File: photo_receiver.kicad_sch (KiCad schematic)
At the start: 9 parts

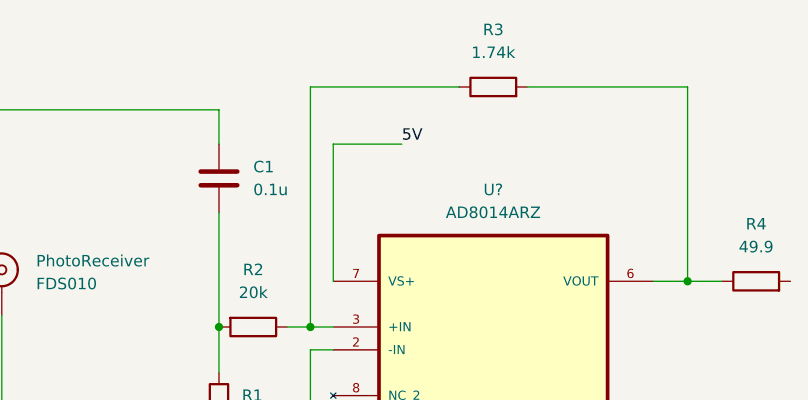
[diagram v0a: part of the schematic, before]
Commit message: Added power supply and standardised on pwer supply net names
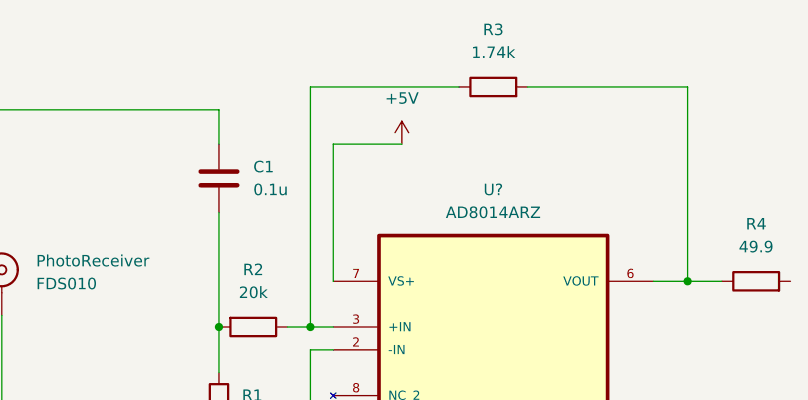
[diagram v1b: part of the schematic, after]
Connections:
- net 5V renamed +5V
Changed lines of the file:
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@@
     (stroke (width 0) (type default) (color 0 0 0 0))
-  )
-  (label "5V" (at 172.72 72.39 0)
-    (effects (font (size 1.27 1.27)) (justify left bottom))
   )
   (symbol (lib_id "local_library:AD8014ARZ") (at 182.88 95.25 0) (unit 1)
@@
     (pin "2")
   )
+  (symbol (lib_id "power:+5V") (at 172.72 72.39 0) (unit 1)
+    (in_bom yes) (on_board yes) (fields_autoplaced)
+    (property "Reference" "#PWR?" (id 0) (at 172.72 76.2 0)
+      (effects (font (size 1.27 1.27)) hide)
+    )
+    (property "Value" "+5V" (id 1) (at 172.72 67.31 0))
+    (property "Footprint" "" (id 2) (at 172.72 72.39 0)
+      (effects (font (size 1.27 1.27)) hide)
+    )
+    (property "Datasheet" "" (id 3) (at 172.72 72.39 0)
+      (effects (font (size 1.27 1.27)) hide)
+    )
+    (pin "1")
+  )
 )

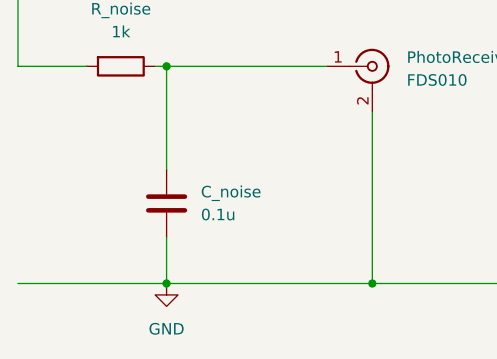
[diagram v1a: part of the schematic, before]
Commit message: improve labels on comparator
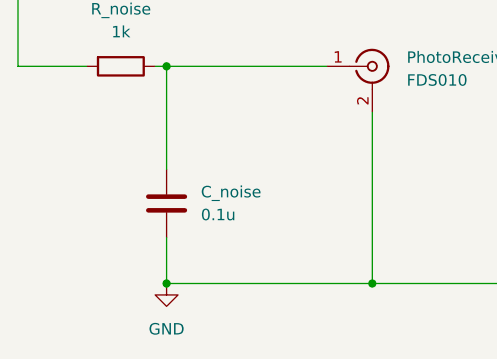
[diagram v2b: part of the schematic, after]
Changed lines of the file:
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@@
   (junction (at 105.41 86.36) (diameter 0) (color 0 0 0 0)
-  )
-  (wire (pts (xy 88.9 110.49) (xy 105.41 110.49))
-    (stroke (width 0) (type default) (color 0 0 0 0))
   )
   (wire (pts (xy 165.1 95.25) (xy 162.56 95.25))

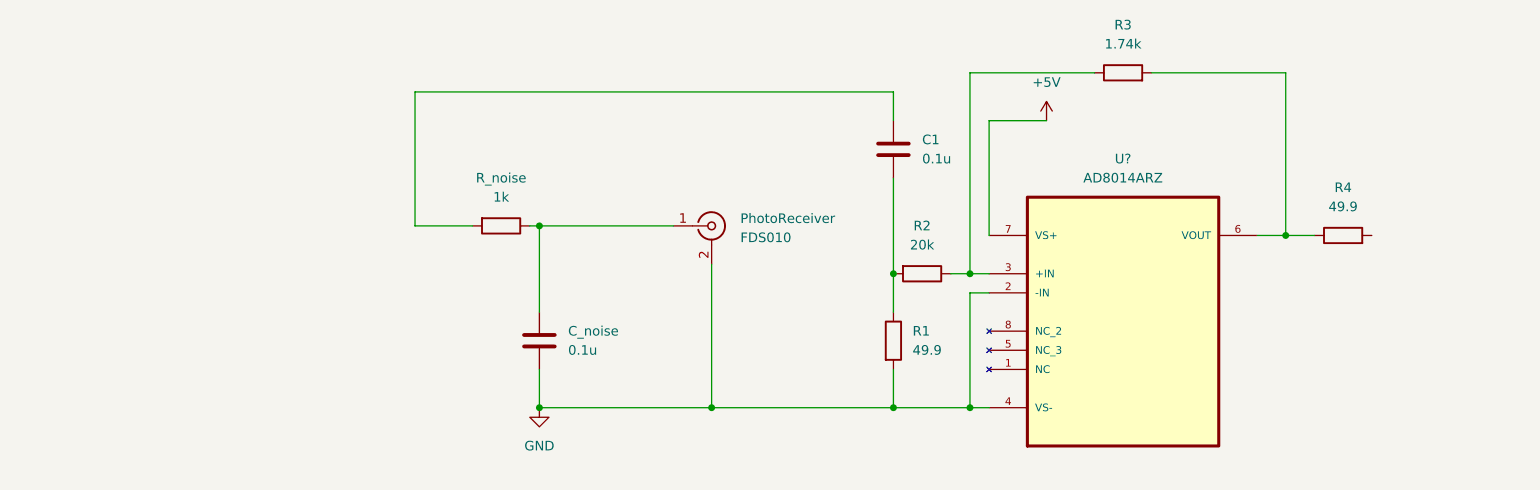
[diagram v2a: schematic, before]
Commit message: add component numbers to schematic
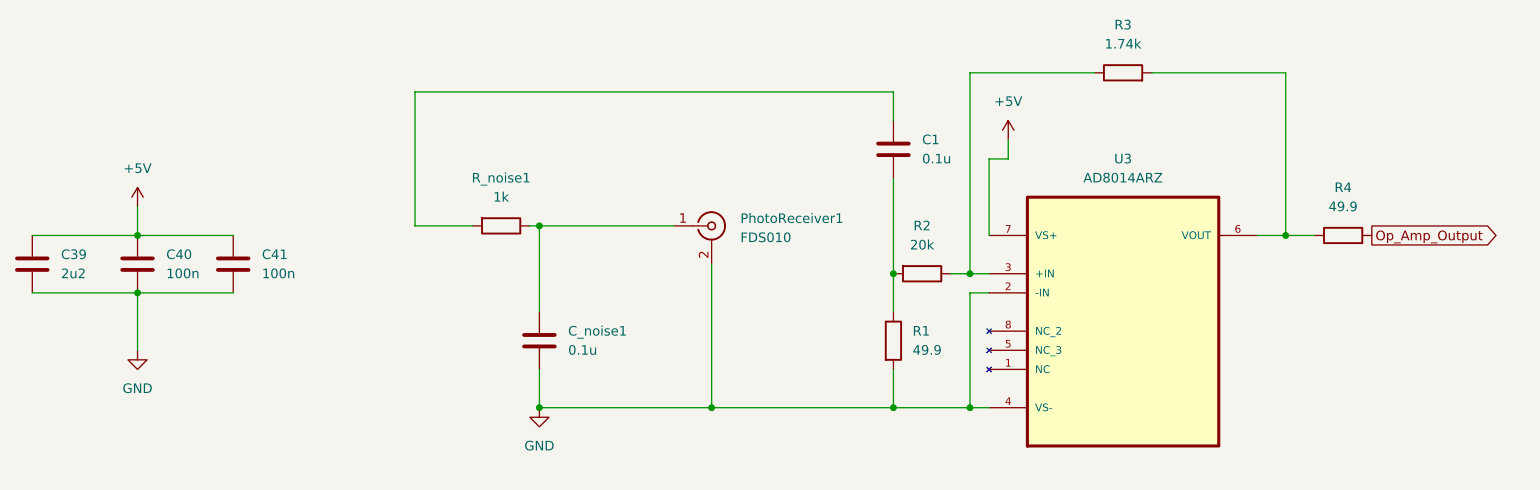
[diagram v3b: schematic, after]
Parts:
- added C39: 2u2, symbol Device:C
- added C40, C41: 100n, symbol Device:C
- gave numbers to parts that had none: 1
- renumbered C_noise to C_noise1, PhotoReceiver to PhotoReceiver1, R_noise to R_noise1
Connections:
- net +5V: now also C39.1, C40.1, C41.1
- net GND: now also C39.2, C40.2, C41.2
- net Op_Amp_Output: now reaches R4.2
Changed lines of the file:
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@@
 (kicad_sch (version 20211123) (generator eeschema)
   (paper "A4")
+  (junction (at 52.07 87.63) (diameter 0) (color 0 0 0 0)
+  )
   (junction (at 105.41 110.49) (diameter 0) (color 0 0 0 0)
   )
   (junction (at 162.56 110.49) (diameter 0) (color 0 0 0 0)
   )
+  (junction (at 52.07 95.25) (diameter 0) (color 0 0 0 0)
+  )
   (junction (at 152.4 110.49) (diameter 0) (color 0 0 0 0)
   )
@@
     (stroke (width 0) (type default) (color 0 0 0 0))
   )
+  (wire (pts (xy 167.64 77.47) (xy 165.1 77.47))
+    (stroke (width 0) (type default) (color 0 0 0 0))
+  )
   (wire (pts (xy 105.41 110.49) (xy 128.27 110.49))
     (stroke (width 0) (type default) (color 0 0 0 0))
@@
     (stroke (width 0) (type default) (color 0 0 0 0))
   )
+  (wire (pts (xy 52.07 83.82) (xy 52.07 87.63))
+    (stroke (width 0) (type default) (color 0 0 0 0))
+  )
   (wire (pts (xy 152.4 68.58) (xy 88.9 68.58))
     (stroke (width 0) (type default) (color 0 0 0 0))
   )
-  (wire (pts (xy 165.1 87.63) (xy 165.1 72.39))
-    (stroke (width 0) (type default) (color 0 0 0 0))
-  )
   (wire (pts (xy 105.41 86.36) (xy 123.19 86.36))
     (stroke (width 0) (type default) (color 0 0 0 0))
@@
     (stroke (width 0) (type default) (color 0 0 0 0))
   )
-  (wire (pts (xy 165.1 72.39) (xy 172.72 72.39))
+  (wire (pts (xy 167.64 74.93) (xy 167.64 77.47))
+    (stroke (width 0) (type default) (color 0 0 0 0))
+  )
+  (wire (pts (xy 52.07 87.63) (xy 64.77 87.63))
     (stroke (width 0) (type default) (color 0 0 0 0))
   )
@@
     (stroke (width 0) (type default) (color 0 0 0 0))
   )
+  (wire (pts (xy 38.1 87.63) (xy 52.07 87.63))
+    (stroke (width 0) (type default) (color 0 0 0 0))
+  )
   (wire (pts (xy 162.56 92.71) (xy 165.1 92.71))
     (stroke (width 0) (type default) (color 0 0 0 0))
@@
     (stroke (width 0) (type default) (color 0 0 0 0))
   )
+  (wire (pts (xy 52.07 95.25) (xy 52.07 102.87))
+    (stroke (width 0) (type default) (color 0 0 0 0))
+  )
   (wire (pts (xy 162.56 66.04) (xy 179.07 66.04))
     (stroke (width 0) (type default) (color 0 0 0 0))
@@
     (stroke (width 0) (type default) (color 0 0 0 0))
   )
+  (wire (pts (xy 38.1 95.25) (xy 52.07 95.25))
+    (stroke (width 0) (type default) (color 0 0 0 0))
+  )
   (wire (pts (xy 204.47 66.04) (xy 204.47 87.63))
     (stroke (width 0) (type default) (color 0 0 0 0))
   )
+  (wire (pts (xy 52.07 95.25) (xy 64.77 95.25))
+    (stroke (width 0) (type default) (color 0 0 0 0))
+  )
+  (wire (pts (xy 165.1 77.47) (xy 165.1 87.63))
+    (stroke (width 0) (type default) (color 0 0 0 0))
+  )
   (wire (pts (xy 128.27 110.49) (xy 152.4 110.49))
     (stroke (width 0) (type default) (color 0 0 0 0))
   )
+  (global_label "Op_Amp_Output" (shape output) (at 215.9 87.63 0) (fields_autoplaced)
+    (effects (font (size 1.27 1.27)) (justify left))
+    (property "Intersheet References" "${INTERSHEET_REFS}" (id 0) (at 232.8879 87.5506 0)
+      (effects (font (size 1.27 1.27)) (justify left) hide)
+    )
+  )
   (symbol (lib_id "local_library:AD8014ARZ") (at 182.88 95.25 0) (unit 1)
     (in_bom yes) (on_board yes) (fields_autoplaced)
-    (property "Reference" "U?" (id 0) (at 182.88 77.47 0))
+    (property "Reference" "U3" (id 0) (at 182.88 77.47 0))
     (property "Value" "AD8014ARZ" (id 1) (at 182.88 80.01 0))
     (property "Footprint" "SOIC127P600X175-8N" (id 2) (at 182.88 85.09 0)
@@
   (symbol (lib_id "power:GND") (at 105.41 110.49 0) (unit 1)
     (in_bom yes) (on_board yes) (fields_autoplaced)
-    (property "Reference" "#PWR?" (id 0) (at 105.41 116.84 0)
+    (property "Reference" "#PWR038" (id 0) (at 105.41 116.84 0)
       (effects (font (size 1.27 1.27)) hide)
     )
@@
     )
     (property "Datasheet" "~" (id 3) (at 152.4 76.2 0)
+      (effects (font (size 1.27 1.27)) hide)
+    )
+    (pin "1")
+    (pin "2")
+  )
+  (symbol (lib_id "Device:C") (at 64.77 91.44 0) (unit 1)
+    (in_bom yes) (on_board yes) (fields_autoplaced)
+    (property "Reference" "C41" (id 0) (at 68.58 90.1699 0)
+      (effects (font (size 1.27 1.27)) (justify left))
+    )
+    (property "Value" "100n" (id 1) (at 68.58 92.7099 0)
+      (effects (font (size 1.27 1.27)) (justify left))
+    )
+    (property "Footprint" "" (id 2) (at 65.7352 95.25 0)
+      (effects (font (size 1.27 1.27)) hide)
+    )
+    (property "Datasheet" "~" (id 3) (at 64.77 91.44 0)
       (effects (font (size 1.27 1.27)) hide)
     )
@@
   (symbol (lib_id "Connector:Conn_Coaxial") (at 128.27 86.36 0) (unit 1)
     (in_bom yes) (on_board yes) (fields_autoplaced)
-    (property "Reference" "PhotoReceiver" (id 0) (at 132.08 85.3831 0)
+    (property "Reference" "PhotoReceiver1" (id 0) (at 132.08 85.3831 0)
       (effects (font (size 1.27 1.27)) (justify left))
     )
@@
   (symbol (lib_id "Device:C") (at 105.41 101.6 0) (unit 1)
     (in_bom yes) (on_board yes) (fields_autoplaced)
-    (property "Reference" "C_noise" (id 0) (at 109.22 100.3299 0)
+    (property "Reference" "C_noise1" (id 0) (at 109.22 100.3299 0)
       (effects (font (size 1.27 1.27)) (justify left))
     )
@@
   (symbol (lib_id "Device:R") (at 100.33 86.36 270) (unit 1)
     (in_bom yes) (on_board yes) (fields_autoplaced)
-    (property "Reference" "R_noise" (id 0) (at 100.33 80.01 90))
+    (property "Reference" "R_noise1" (id 0) (at 100.33 80.01 90))
     (property "Value" "1k" (id 1) (at 100.33 82.55 90))
     (property "Footprint" "" (id 2) (at 100.33 84.582 90)
@@
     (pin "2")
   )
-  (symbol (lib_id "power:+5V") (at 172.72 72.39 0) (unit 1)
-    (in_bom yes) (on_board yes) (fields_autoplaced)
-    (property "Reference" "#PWR?" (id 0) (at 172.72 76.2 0)
-      (effects (font (size 1.27 1.27)) hide)
-    )
-    (property "Value" "+5V" (id 1) (at 172.72 67.31 0))
-    (property "Footprint" "" (id 2) (at 172.72 72.39 0)
-      (effects (font (size 1.27 1.27)) hide)
-    )
-    (property "Datasheet" "" (id 3) (at 172.72 72.39 0)
-      (effects (font (size 1.27 1.27)) hide)
-    )
+  (symbol (lib_id "Device:C") (at 52.07 91.44 0) (unit 1)
+    (in_bom yes) (on_board yes) (fields_autoplaced)
+    (property "Reference" "C40" (id 0) (at 55.88 90.1699 0)
+      (effects (font (size 1.27 1.27)) (justify left))
+    )
+    (property "Value" "100n" (id 1) (at 55.88 92.7099 0)
+      (effects (font (size 1.27 1.27)) (justify left))
+    )
+    (property "Footprint" "" (id 2) (at 53.0352 95.25 0)
+      (effects (font (size 1.27 1.27)) hide)
+    )
+    (property "Datasheet" "~" (id 3) (at 52.07 91.44 0)
+      (effects (font (size 1.27 1.27)) hide)
+    )
+    (pin "1")
+    (pin "2")
+  )
+  (symbol (lib_id "power:+5V") (at 52.07 83.82 0) (unit 1)
+    (in_bom yes) (on_board yes) (fields_autoplaced)
+    (property "Reference" "#PWR052" (id 0) (at 52.07 87.63 0)
+      (effects (font (size 1.27 1.27)) hide)
+    )
+    (property "Value" "+5V" (id 1) (at 52.07 78.74 0))
+    (property "Footprint" "" (id 2) (at 52.07 83.82 0)
+      (effects (font (size 1.27 1.27)) hide)
+    )
+    (property "Datasheet" "" (id 3) (at 52.07 83.82 0)
+      (effects (font (size 1.27 1.27)) hide)
+    )
+    (pin "1")
+  )
+  (symbol (lib_id "power:GND") (at 52.07 102.87 0) (unit 1)
+    (in_bom yes) (on_board yes) (fields_autoplaced)
+    (property "Reference" "#PWR053" (id 0) (at 52.07 109.22 0)
+      (effects (font (size 1.27 1.27)) hide)
+    )
+    (property "Value" "GND" (id 1) (at 52.07 107.95 0))
+    (property "Footprint" "" (id 2) (at 52.07 102.87 0)
+      (effects (font (size 1.27 1.27)) hide)
+    )
+    (property "Datasheet" "" (id 3) (at 52.07 102.87 0)
+      (effects (font (size 1.27 1.27)) hide)
+    )
+    (pin "1")
+  )
+  (symbol (lib_id "Device:C") (at 38.1 91.44 0) (unit 1)
+    (in_bom yes) (on_board yes) (fields_autoplaced)
+    (property "Reference" "C39" (id 0) (at 41.91 90.1699 0)
+      (effects (font (size 1.27 1.27)) (justify left))
+    )
+    (property "Value" "2u2" (id 1) (at 41.91 92.7099 0)
+      (effects (font (size 1.27 1.27)) (justify left))
+    )
+    (property "Footprint" "" (id 2) (at 39.0652 95.25 0)
+      (effects (font (size 1.27 1.27)) hide)
+    )
+    (property "Datasheet" "~" (id 3) (at 38.1 91.44 0)
+      (effects (font (size 1.27 1.27)) hide)
+    )
+    (pin "1")
+    (pin "2")
+  )
+  (symbol (lib_id "power:+5V") (at 167.64 74.93 0) (unit 1)
+    (in_bom yes) (on_board yes) (fields_autoplaced)
+    (property "Reference" "#PWR039" (id 0) (at 167.64 78.74 0)
+      (effects (font (size 1.27 1.27)) hide)
+    )
+    (property "Value" "+5V" (id 1) (at 167.64 69.85 0))
+    (property "Footprint" "" (id 2) (at 167.64 74.93 0)
+      (effects (font (size 1.27 1.27)) hide)
+    )
+    (property "Datasheet" "" (id 3) (at 167.64 74.93 0)
+      (effects (font (size 1.27 1.27)) hide)
+    )

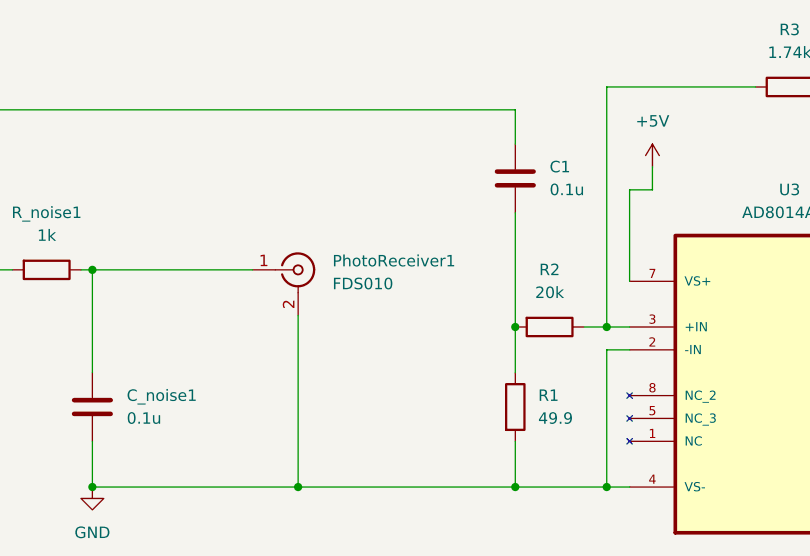
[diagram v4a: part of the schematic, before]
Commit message: Add footprints to SMA connectors and FPGA
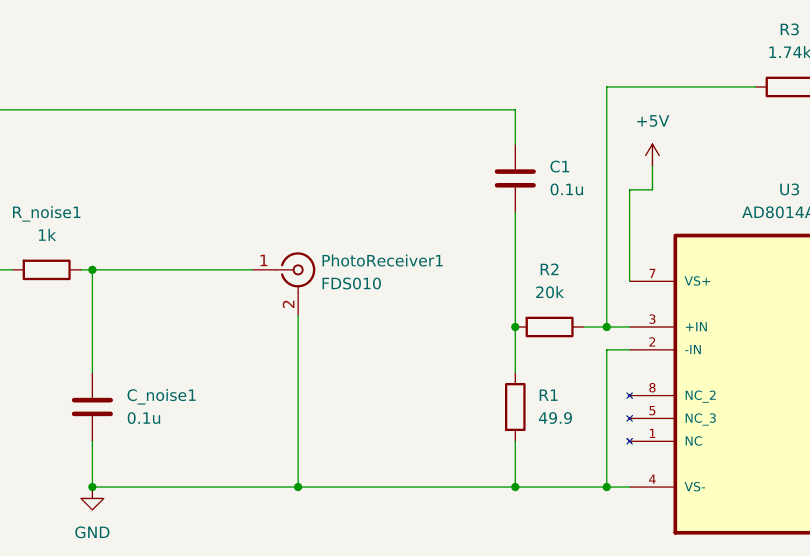
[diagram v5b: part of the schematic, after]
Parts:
- PhotoReceiver1: footprint (none) -> Connector_Coaxial:SMA_Amphenol_901-144_Vertical
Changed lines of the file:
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@@
   (symbol (lib_id "Connector:Conn_Coaxial") (at 128.27 86.36 0) (unit 1)
     (in_bom yes) (on_board yes) (fields_autoplaced)
-    (property "Reference" "PhotoReceiver1" (id 0) (at 132.08 85.3831 0)
+    (property "Reference" "PhotoReceiver1" (id 0) (at 130.81 85.3831 0)
       (effects (font (size 1.27 1.27)) (justify left))
     )
-    (property "Value" "FDS010" (id 1) (at 132.08 87.9231 0)
+    (property "Value" "FDS010" (id 1) (at 130.81 87.9231 0)
       (effects (font (size 1.27 1.27)) (justify left))
     )
-    (property "Footprint" "" (id 2) (at 128.27 86.36 0)
+    (property "Footprint" "Connector_Coaxial:SMA_Amphenol_901-144_Vertical" (id 2) (at 128.27 86.36 0)
       (effects (font (size 1.27 1.27)) hide)
     )

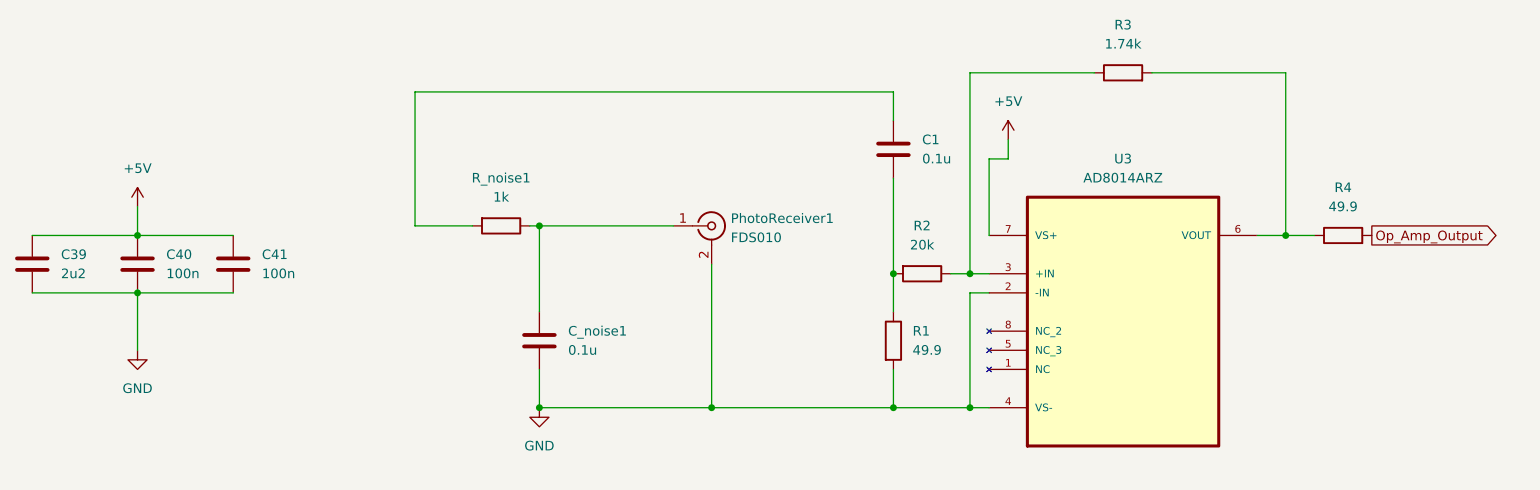
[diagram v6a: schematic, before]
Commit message: Fixed Receiver schematic
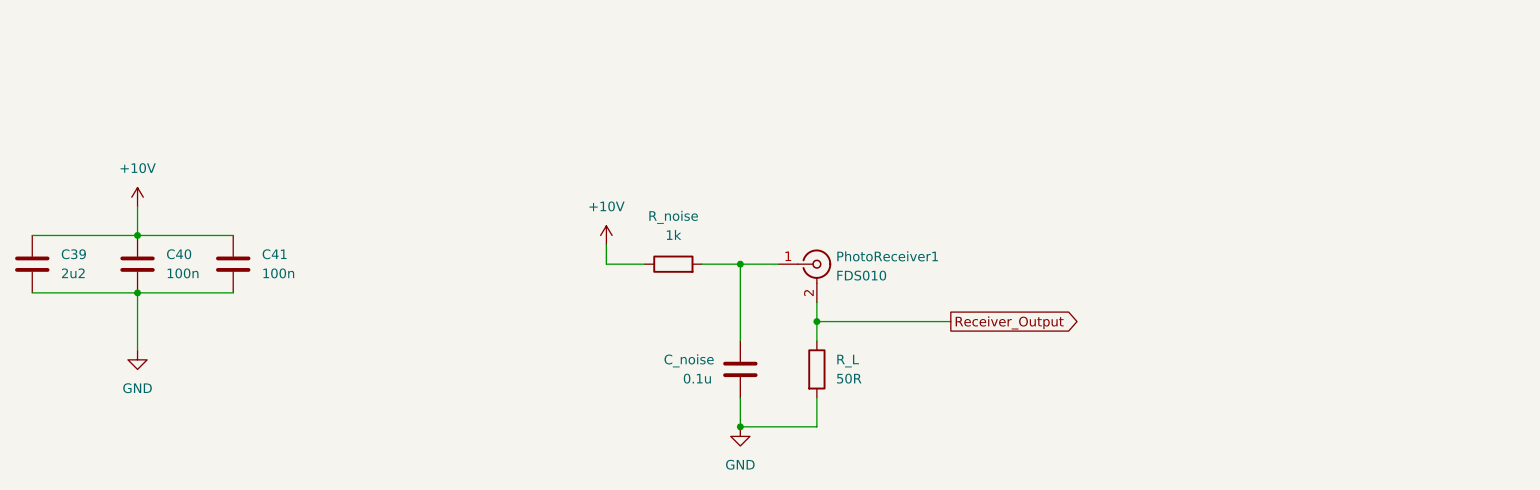
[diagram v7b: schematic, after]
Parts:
- removed C1, C_noise1: 0.1u, symbol Device:C
- removed R1, R4: 49.9, symbol Device:R
- removed R2: 20k, symbol Device:R
- removed R3: 1.74k, symbol Device:R
- removed R_noise1: 1k, symbol Device:R
- removed U3: AD8014ARZ, SOIC127P600X175-8N, symbol local_library:AD8014ARZ
- added C_noise: 0.1u, symbol Device:C
- added R_L: 50R, symbol Device:R
- added R_noise: 1k, symbol Device:R
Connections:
- net GND: now also C_noise.2, R_L.2; no longer PhotoReceiver1.2 (Ext)
- net at PhotoReceiver1.1 (In): now also C_noise.1, R_noise.2
- net +5V renamed +10V
- net +10V: now also R_noise.1
- new net Receiver_Output: PhotoReceiver1.2 (Ext), R_L.1
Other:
- moved on the sheet: PhotoReceiver1
